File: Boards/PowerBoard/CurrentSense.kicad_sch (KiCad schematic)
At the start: 44 parts, among them IC10 ACS772ECB-400B-PFF-T, IC3 ACS772ECB-400B-PFF-T, IC4 ACS772ECB-400B-PFF-T, IC5 ACS772ECB-400B-PFF-T, IC6 ACS772ECB-400B-PFF-T, IC7 ACS772ECB-400B-PFF-T, IC8 ACS772ECB-400B-PFF-T, IC9 ACS772ECB-400B-PFF-T

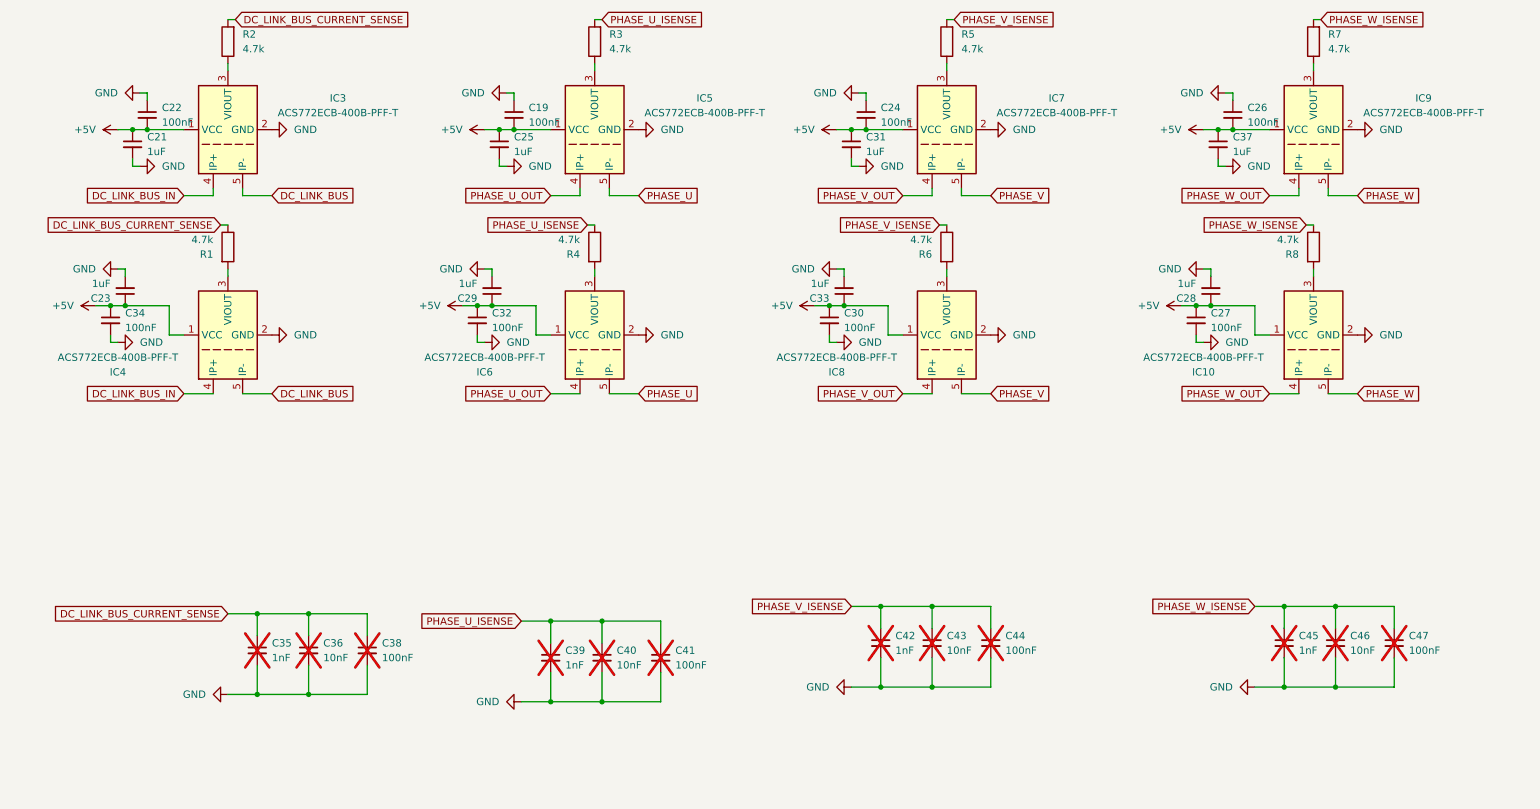
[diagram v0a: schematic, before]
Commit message: Add Zeners to Power Board
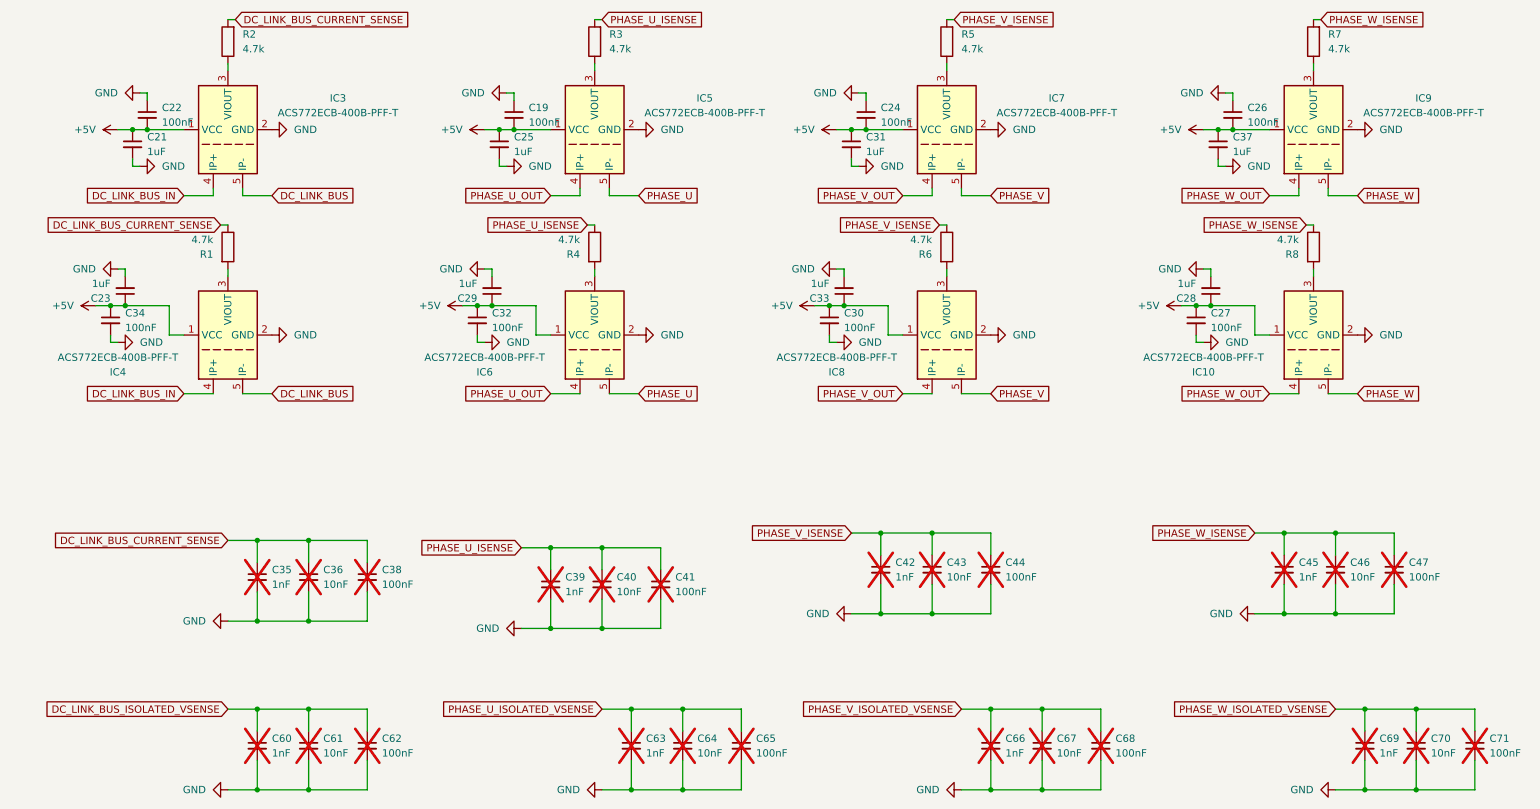
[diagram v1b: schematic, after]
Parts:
- added C60, C63, C66, C69: 1nF, Capacitor_SMD:C_1210_3225Metric_Pad1.33x2.70mm_HandSolder, symbol Device:C_Small
- added C61, C64, C67, C70: 10nF, Capacitor_SMD:C_1210_3225Metric_Pad1.33x2.70mm_HandSolder, symbol Device:C_Small
- added C62, C65, C68, C71: 100nF, Capacitor_SMD:C_1210_3225Metric_Pad1.33x2.70mm_HandSolder, symbol Device:C_Small
- C36, C38, C40, C41, C43, C44, C46, C47: footprint Capacitor_SMD:C_1210_3225Metric_Pad1.33x2.70mm_HandSolde -> Capacitor_SMD:C_1210_3225Metric_Pad1.33x2.70mm_HandSolder
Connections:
- net GND: now also C60.2, C61.2, C62.2, C63.2, C64.2, C65.2, C66.2, C67.2, C68.2, C69.2, C70.2, C71.2
- new net DC_LINK_BUS_ISOLATED_VSENSE: C60.1, C61.1, C62.1
- new net PHASE_U_ISOLATED_VSENSE: C63.1, C64.1, C65.1
- new net PHASE_V_ISOLATED_VSENSE: C66.1, C67.1, C68.1
- new net PHASE_W_ISOLATED_VSENSE: C69.1, C70.1, C71.1
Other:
- moved on the sheet: C35, C36, C38, C39, C40, C41, C42, C43, C44, C45, C46, C47

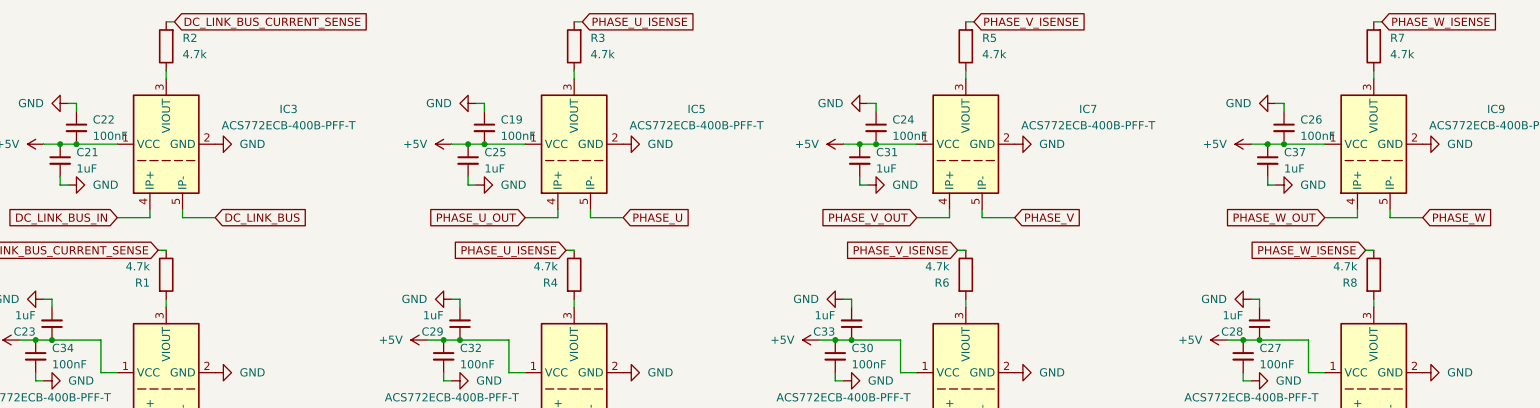
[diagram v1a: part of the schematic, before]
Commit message: Update Dynamic Brake Board
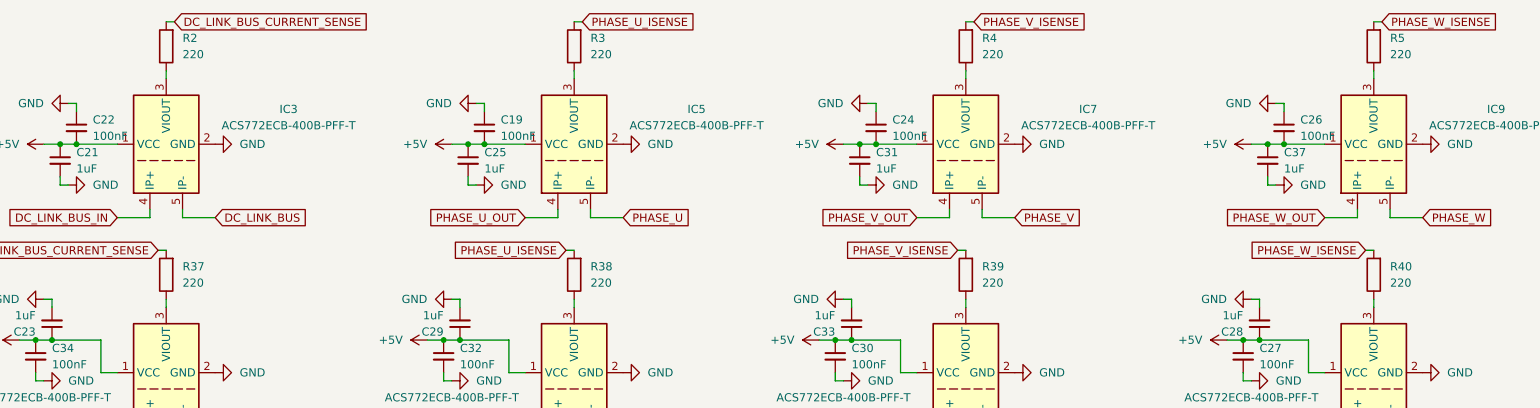
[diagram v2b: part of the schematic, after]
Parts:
- removed R1, R6, R7, R8: 4.7k, Resistor_SMD:R_1210_3225Metric_Pad1.30x2.65mm_HandSolder, symbol Device:R
- added R37, R38, R39, R40: 220, Resistor_SMD:R_1210_3225Metric_Pad1.30x2.65mm_HandSolder, symbol Device:R
- R2, R3, R4, R5: value 4.7k -> 220
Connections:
- net DC_LINK_BUS_CURRENT_SENSE: now also R37.2
- net PHASE_U_ISENSE: now also R38.2; no longer R4.1
- net PHASE_V_ISENSE: now also R4.2, R39.2; no longer R5.2
- net PHASE_W_ISENSE: now also R5.2, R40.2
- net at IC10.3 (VIOUT): now also R40.1
- net at IC8.3 (VIOUT): now also R39.1
- net at IC9.3 (VIOUT): now also R5.1
- net at IC7.3 (VIOUT): now also R4.1; no longer R5.1
- net at IC4.3 (VIOUT): now also R37.1
- net at IC6.3 (VIOUT): now also R38.1; no longer R4.2
